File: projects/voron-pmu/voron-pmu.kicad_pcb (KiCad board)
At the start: 2 copper layers, 131 x 64.5 mm, 13 parts, among them J1 Critical loads, J2 Non-critical loads, J3 Critical supply, J4 Non-critical supply, J5 Pwr-loss-1, J6 Pwr-loss-2, K1 FINDER-40.52, K2 FINDER-40.52, K3 FINDER-40.52, K4 FINDER-40.52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

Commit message: Re-saving.
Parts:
- J5: footprint Connector_Phoenix_MC:PhoenixContact_MCV_1,5_3-G-3.5_1x03_P3.50mm_Vertical -> Connector_JST:JST_XH_B3B-XH-A_1x03_P2.50mm_Vertical
- moved K3 48.5 mm to (133.8, 110.4), turned to 90 degrees
- moved J6 22.7 mm to (104.4, 96.0), turned to -90 degrees
- moved J5 22.1 mm to (104.5, 82.5), turned to -90 degrees
- moved PS2 2.92 mm to (156.0, 77.9)
- moved K4 0.50 mm to (149.2, 110.4)
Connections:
- PS2 pad 5: unconnected-(PS2-AC(L)-Pad5) -> Net-(J3-Pin_1)
- PS2 pad 6: unconnected-(PS2-AC(N)-Pad6) -> Net-(J3-Pin_2)
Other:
- board size 131 x 64.5 mm -> 104 x 64.5 mm

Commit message: Prettyfing schematics.
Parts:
- added H1: MountingHole, MountingHole:MountingHole_3.2mm_M3, F.Cu at (100.0, 50.0)
- added H2: MountingHole, MountingHole:MountingHole_3.2mm_M3, F.Cu at (200.0, 50.0)
- added H3: MountingHole, MountingHole:MountingHole_3.2mm_M3, F.Cu at (200.0, 115.0)
- added H4: MountingHole, MountingHole:MountingHole_3.2mm_M3, F.Cu at (100.0, 115.0)
- J6: footprint Connector_Phoenix_MC:PhoenixContact_MCV_1,5_3-G-3.5_1x03_P3.50mm_Vertical -> Connector_JST:JST_XH_B3B-XH-A_1x03_P2.50mm_Vertical
- SW1: value SW_Push -> sw-on; footprint Connector_Phoenix_MC:PhoenixContact_MCV_1,5_2-G-3.5_1x02_P3.50mm_Vertical -> Connector_JST:JST_XH_B2B-XH-A_1x02_P2.50mm_Vertical
- SW2: value SW_Push_Open -> sw-off; footprint Connector_Phoenix_MC:PhoenixContact_MCV_1,5_2-G-3.5_1x02_P3.50mm_Vertical -> Connector_JST:JST_XH_B2B-XH-A_1x02_P2.50mm_Vertical
- moved J1 14.8 mm to (199.0, 76.5)
- moved J3 14.6 mm to (199.0, 63.1)
- moved J5 9.66 mm to (101.0, 91.5)
- moved J6 7.75 mm to (101.0, 103.0)
- moved J2 5.39 mm to (199.0, 107.0)
- moved J4 5.39 mm to (199.0, 93.5)
- moved SW1 5.15 mm to (101.0, 65.5), turned to -90 degrees
- moved SW2 4.80 mm to (101.0, 56.5), turned to -90 degrees
- moved K1 4.53 mm to (164.5, 75.0)
- moved K2 4.53 mm to (171.8, 81.6)
- moved K3 4.53 mm to (133.2, 105.9)
- moved K4 4.53 mm to (148.8, 105.9)
- moved PS2 4.53 mm to (155.5, 73.4)
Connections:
- net power-good renamed +24V-sw
- PS2 pad 5: Net-(J3-Pin_1) -> Net-(J3-Pin_2)
- PS2 pad 6: Net-(J3-Pin_2) -> Net-(J3-Pin_1)
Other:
- board size 104 x 64.5 mm -> 107 x 72 mm

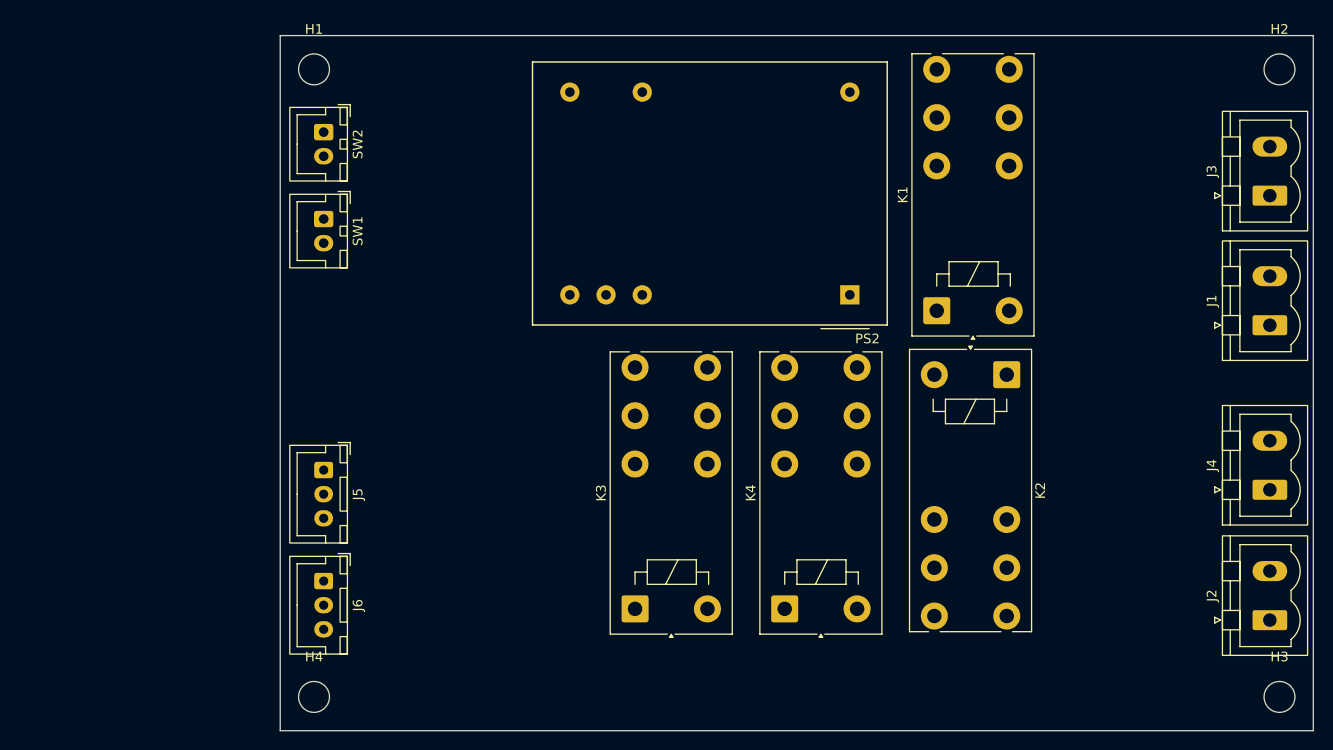
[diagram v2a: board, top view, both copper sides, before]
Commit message: Replacing relays with Omron. Will route now.
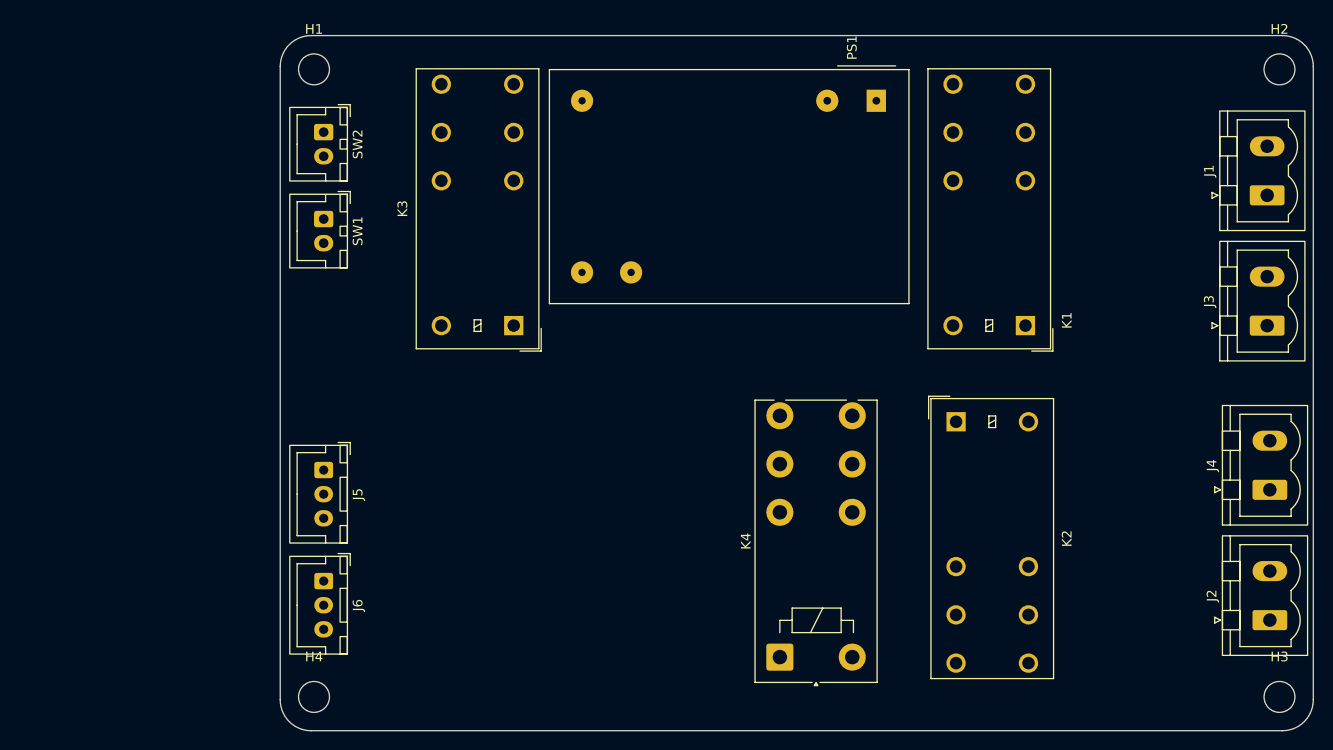
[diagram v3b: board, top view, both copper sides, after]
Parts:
- K1, K2, K3: value FINDER-40.52 -> G2RL-2; footprint Relay_THT:Relay_DPDT_Finder_40.52 -> Relay_THT:Relay_DPDT_Omron_G2RL-2
- PS1: renamed from PS2; value TMLM04124 -> IRM-03-24; footprint Converter_ACDC:Converter_ACDC_TRACO_TMLM-04_THT -> Converter_ACDC:Converter_ACDC_MeanWell_IRM-03-xx_THT
- moved K3 31.9 mm to (120.7, 76.5), turned to 180 degrees
- moved PS1 20.3 mm to (158.2, 53.3), turned to -90 degrees
- moved J3 13.5 mm to (198.7, 76.5)
- moved J1 13.5 mm to (198.7, 63.0)
- moved K1 9.32 mm to (173.7, 76.5), turned to 180 degrees
- moved K2 7.17 mm to (166.5, 86.5), turned to 0 degrees
- moved K4 5.02 mm to (148.2, 110.9)
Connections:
- PS1 pad 1: (no net) -> Net-(J3-Pin_2)
- PS1 pad 3: GND -> Net-(J3-Pin_1)
- PS1 pad 5: Net-(J3-Pin_2) -> unconnected-(PS1-NC-Pad5)
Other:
- outline, holes or cut-outs redrawn

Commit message: Battling Mouser and Kicad.
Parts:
- PS1: value IRM-03-24 -> RAC05-24SK; footprint Converter_ACDC:Converter_ACDC_MeanWell_IRM-03-xx_THT -> Converter_ACDC:Converter_ACDC_RECOM_RAC05-xxSK_THT
- moved PS1 13.9 mm to (157.5, 67.2), turned to 0 degrees
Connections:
- PS1 pad 3: Net-(J3-Pin_1) -> unconnected-(PS1-NC-Pad3)
- PS1 pad 5: unconnected-(PS1-NC-Pad5) -> +24V
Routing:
- net GND: track 0.00 -> 102.2 mm
- net +24V-sw: track 0.00 -> 83.3 mm
- net Net-(J3-Pin_1): track 0.00 -> 79.2 mm
- net Net-(J6-Pin_1): track 0.00 -> 65.3 mm
- net Net-(J2-Pin_2): track 0.00 -> 64.2 mm
- net Net-(J6-Pin_2): track 0.00 -> 62.5 mm
- net Net-(J6-Pin_3): track 0.00 -> 59.8 mm
- net Net-(J2-Pin_1): track 0.00 -> 53.6 mm
- net +24V: track 0.00 -> 53.5 mm
- net Net-(J4-Pin_1): track 0.00 -> 51.2 mm
- net Net-(K3-Pad11): track 0.00 -> 49.8 mm
- net Net-(J5-Pin_1): track 0.00 -> 49.6 mm
- net Net-(J3-Pin_2): track 0.00 -> 49.3 mm
- net Net-(J5-Pin_2): track 0.00 -> 48.5 mm
- net Net-(J5-Pin_3): track 0.00 -> 47.5 mm
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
